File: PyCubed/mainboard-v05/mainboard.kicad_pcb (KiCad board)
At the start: 4 copper layers, 90.2 x 95.9 mm, 275 parts, among them J1 503182-1852, J10 Conn_01x04, J11 874370343, J12 Amphenol_901-144, J13 USB_C_pycubed, J14 Conn_01x06, J15 Conn_01x02, J16 1985807, J17 1985807, J18 1985807, J19 874370343, J2 Conn_01x05, J20 874370343, J21 874370343, J22 874370343, J23 874370343, J24 MOLEX_Sherlock_2pos, J3 MOLEX_Sherlock_2pos, J4 874370443, J5 Amphenol_901-144, J6 Amphenol_901-144, J7 Amphenol_901-144, J8 Conn_01x09, J9 Conn_01x03, Q1 IRLML2803, Q10 MBT2222ADW1T1, Q11 MMDT2907, Q12 BSS138DWQ-7, Q13 BSS138DWQ-7, Q14 BSS138DWQ-7, Q15 MBT2222ADW1T1, Q16 MBT2222ADW1T1, Q17 MMBT2907, Q18 BSS138DWQ-7, Q19 BSS138DWQ-7, Q2 MBT2222ADW1T1, Q20 NDS8434, Q21 NDS8434, Q22 NDS8434, Q23 MBT2222ADW1T1, Q24 BSS138DWQ-7, Q25 MBT2222ADW1T1, Q26 BSS138DWQ-7, Q27 MBT2222ADW1T1, Q3 MBT2222ADW1T1, Q4 IRLML2803, Q5 IRLML2803, Q6 MMBT2222AT, Q7 MBT2222ADW1T1, Q8 MBT2222ADW1T1, Q9 BSS138DWQ-7, SW1 KMR231NG LFS, U1 MAX706RESA, U13 EP2W+, U14 S1216V8, U15 RFM9xBreakout, U16 PE014006, U17 BQ25883RGER, U2 ATSAMD51J19A-AU, U21 TPS7A4501DCQT, U23 RFM98PW, U24 RFM98PW, U3 BMX160, U4 ADM1176-1ARMZ-R7, U5 TPS54226PWPRPWP14_2P31X2P46-L, U6 LTC4121, U7 KF50BD-TR, U8 MR25H40MDF, U9 TPS54226PWPRPWP14_2P31X2P46-L, Y1 32.768kHz

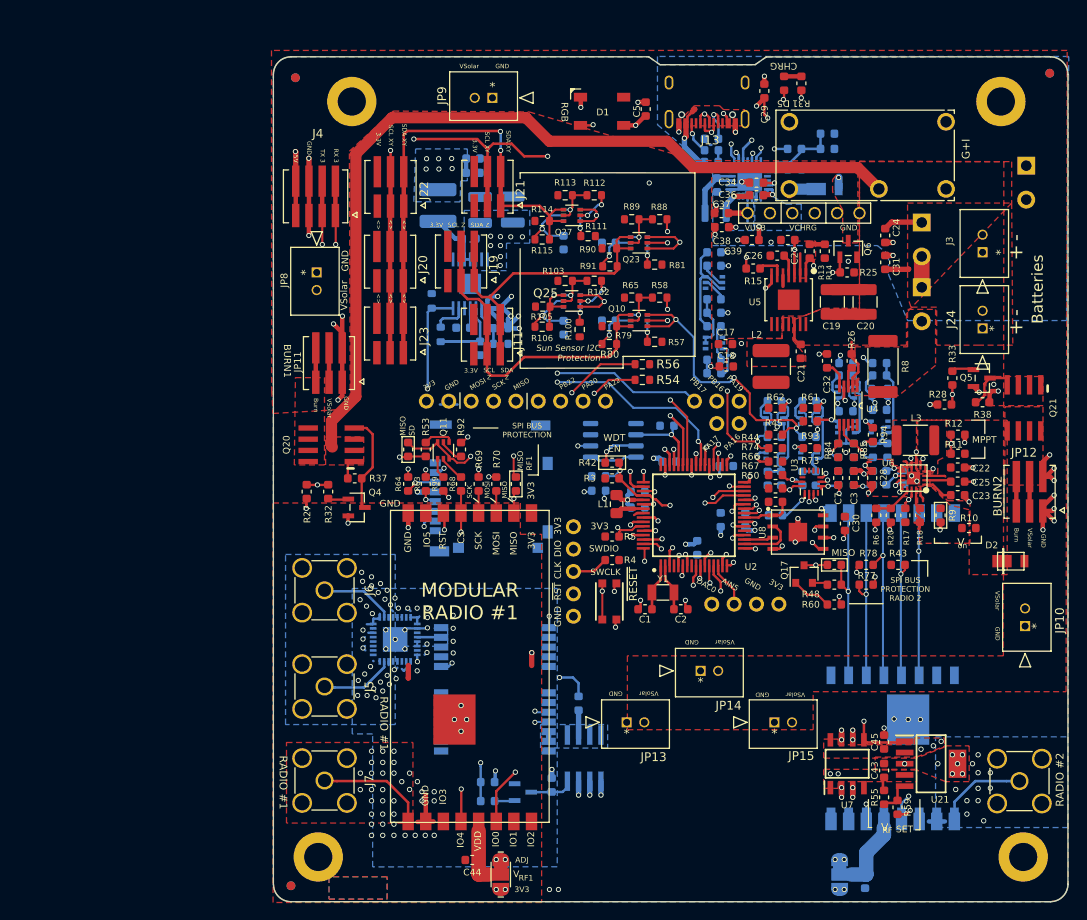
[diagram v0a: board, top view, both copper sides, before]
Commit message: Battery board and side panels ready for CAD check and review, pycubed not finished yet
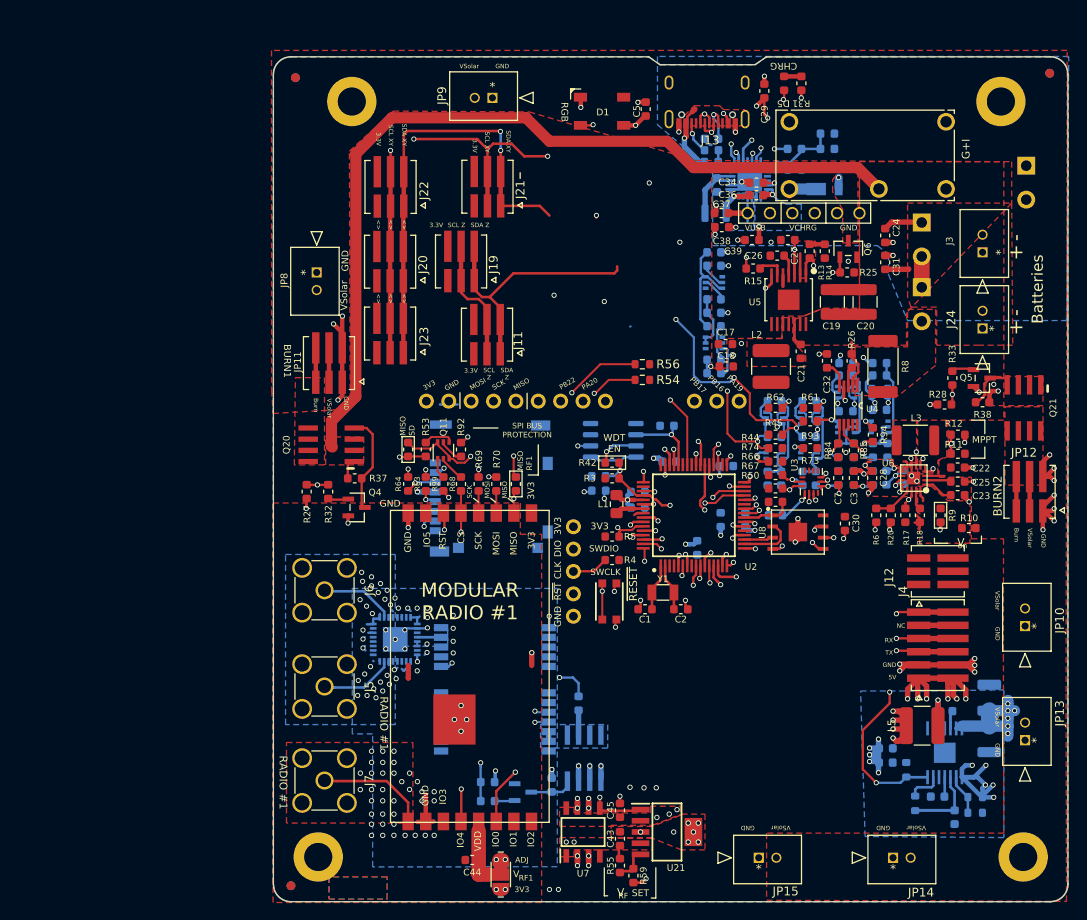
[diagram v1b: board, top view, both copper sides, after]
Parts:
- removed C46: 10uF, Capacitor_SMD:C_0603_1608Metric
- removed C47, C48, C49, C50: 10nF, Capacitor_SMD:C_0603_1608Metric
- removed D2: DFLS130L, mainboard:PWRDI-123
- removed J10: Conn_01x04, Connector_PinHeader_2.54mm:PinHeader_1x04_P2.54mm_Vertical
- removed J15: Conn_01x02, mainboard:PinHeader_CUSTOM3
- removed JP7: Jumper_3_Bridged12, mainboard:SolderJumper-3_P1.3mm_Bridged12_RoundedPad1.0x1.5mm
- removed Q10, Q23, Q25, Q27: MBT2222ADW1T1, Package_TO_SOT_SMD:SOT-363_SC-70-6
- removed Q14, Q24, Q26, Q9: BSS138DWQ-7, mainboard:BSS138DWQ-7
- removed Q17: MMBT2907, Package_TO_SOT_SMD:SOT-23
- removed R100, R111, R57, R81: 100K, Resistor_SMD:R_0603_1608Metric
- removed R102, R112, R58, R88: 680, Resistor_SMD:R_0603_1608Metric
- removed R103, R105, R113, R114, R65, R79, R89, R90: 10K, Resistor_SMD:R_0603_1608Metric
- removed R106, R115, R80, R91: 200K, Resistor_SMD:R_0603_1608Metric
- removed R107, R48: 0, Resistor_SMD:R_0603_1608Metric
- removed R43: 10k, Resistor_SMD:R_0603_1608Metric
- removed R60: 4.7k, Resistor_SMD:R_0603_1608Metric
- removed R77, R78: 1K, Resistor_SMD:R_0603_1608Metric
- removed U15: RFM9xBreakout, RF_Module:HOPERF_RFM9XW_SMD
- removed U24: RFM98PW, mainboard:RFM95PW
- J12: value Amphenol_901-144 -> 874370343; footprint Connector_Coaxial:SMA_Amphenol_901-144_Vertical -> mainboard:MOLEX_874370343
- J4: value 874370443 -> 874370643; footprint mainboard:MOLEX_874370443 -> mainboard:MOLEX_874370643
- L5: moved to F.Cu
- R54, R56: value 4.7K -> 10K
- moved J4 87.1 mm to (173.7, 119.3), turned to 90 degrees
- moved C51 81.7 mm to (167.9, 131.0)
- moved C52 81.7 mm to (167.8, 132.6)
- moved C54 80.8 mm to (179.6, 129.9), turned to 270 degrees
- moved L5 80.6 mm to (172.0, 128.4), turned to 180 degrees
- moved C53 80.0 mm to (179.6, 125.2)
- moved C55 76.2 mm to (174.6, 126.7)
- moved C56 75.7 mm to (173.7, 136.4)
- moved R118 75.7 mm to (178.0, 138.3)
- moved R119 75.7 mm to (171.2, 137.2)
- moved U9 75.7 mm to (174.5, 131.5)
- moved R116 75.7 mm to (170.2, 133.4)
- moved C57 75.7 mm to (175.6, 138.8)
- moved R117 75.7 mm to (178.0, 136.5)
- moved JP13 45.3 mm to (183.6, 130.0), turned to 270 degrees
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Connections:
- net THM renamed Net-(R34-Pad2)
- C22 pad 1: /Power/VCHRG_IN -> VSOLAR
- J11 pad 1_1: SDA_SS_Z -> SDA
- J11 pad 1_2: SDA_SS_Z -> SDA
- J11 pad 2_1: SCL_SS_Z -> SCL
- J11 pad 2_2: SCL_SS_Z -> SCL
- J19 pad 1_1: SDA_SS_Z -> SDA
- J19 pad 1_2: SDA_SS_Z -> SDA
- J19 pad 2_1: SCL_SS_Z -> SCL
- J19 pad 2_2: SCL_SS_Z -> SCL
- J20 pad 1_1: SDA_SS_XY -> SDA_2
- J20 pad 1_2: SDA_SS_XY -> SDA_2
- J20 pad 2_1: SCL_SS_XY -> SCL_2
- J20 pad 2_2: SCL_SS_XY -> SCL_2
- J21 pad 1_1: SDA_SS_XY -> SDA_2
- J21 pad 1_2: SDA_SS_XY -> SDA_2
- J21 pad 2_1: SCL_SS_XY -> SCL_2
- J21 pad 2_2: SCL_SS_XY -> SCL_2
- J22 pad 1_1: SDA_SS_XY -> SDA_2
- J22 pad 1_2: SDA_SS_XY -> SDA_2
- J22 pad 2_1: SCL_SS_XY -> SCL_2
- J22 pad 2_2: SCL_SS_XY -> SCL_2
- J23 pad 1_1: SDA_SS_XY -> SDA_2
- J23 pad 1_2: SDA_SS_XY -> SDA_2
- J23 pad 2_1: SCL_SS_XY -> SCL_2
- J23 pad 2_2: SCL_SS_XY -> SCL_2
- J4 pad 1_1: PB17 -> 5V
- J4 pad 1_2: PB17 -> 5V
- J4 pad 2_1: PB16 -> GND
- J4 pad 2_2: PB16 -> GND
- J4 pad 3_1: GND -> TX_2
- J4 pad 3_2: GND -> TX_2
- J4 pad 4_1: 5V -> RX_2
- J4 pad 4_2: 5V -> RX_2
- J8 pad 8: PA20 -> PB14
- J8 pad 9: PA22 -> (no net)
- J9 pad 3: PA19 -> (no net)
- R10 pad 2: /Power/VCHRG_IN -> VSOLAR
- R11 pad 2: /Power/VCHRG_IN -> VSOLAR
- R116 pad 2: PB23 -> ENAB_CORAL
- R54 pad 2: PA17 -> SCL_2
- R56 pad 2: PA16 -> SDA_2
- U14 pad 22: GPS_PWR_IN -> Net-(U14-Pad22)
- U14 pad 23: GPS_PWR_IN -> Net-(U14-Pad22)
- U2 pad 10: RF2_IO4 -> ENAB_CORAL
- U2 pad 12: RF2_CS -> RST_CORAL
- U2 pad 13: ENAB_RF -> TX_2
- U2 pad 14: AIN5 -> RX_2
- U2 pad 27: RF2_RST -> PB14
- U2 pad 3: DAC0 -> SENSE_THERM
- U2 pad 35: PA16 -> SDA_2
- U2 pad 36: PA17 -> SCL_2
- U2 pad 38: PA19 -> ENAB_RF
- U2 pad 41: PA20 -> (no net)
- U2 pad 43: PA22 -> (no net)
- U2 pad 50: PB23 -> (no net)
- U2 pad 9: RF2_IO0 -> ENAB_THERM
- U6 pad P$3: /Power/VCHRG_IN -> VSOLAR
- U9 pad 7: PB23 -> ENAB_CORAL
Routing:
- net SCL_2: track 0.00 -> 107.9 mm, vias 0 -> 7
- net SDA_2: track 0.00 -> 106.6 mm, vias 0 -> 5
- net SCL_SS_XY: track 76.3 -> 0.00 mm, vias 4 -> 0
- net PB16: track 72.9 -> 8.30 mm, vias 3 -> 1
- net PA16: track 63.9 -> 0.00 mm, vias 3 -> 0
- net PB17: track 67.8 -> 7.61 mm, vias 3 -> 1
- net SDA_SS_XY: track 58.2 -> 0.00 mm, vias 2 -> 0
- net RF2_RST: track 53.6 -> 0.00 mm, vias 2 -> 0
- net ENAB_CORAL: track 0.00 -> 49.6 mm, vias 0 -> 3
- net RF2_CS: track 46.5 -> 0.00 mm, vias 3 -> 0
- net PA17: track 46.4 -> 0.00 mm, vias 3 -> 0
- net PB23: track 44.0 -> 0.00 mm, vias 2 -> 0
- net /Power/V_RF: track 55.0 -> 11.1 mm, vias 6 -> 4
- net RF2_IO4: track 41.8 -> 0.00 mm, vias 2 -> 0
- net SCL_SS_Z: track 39.1 -> 0.00 mm
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- removed copper zone on F.Cu, net /Power/VCHRG_IN
- removed copper zone on B.Cu, net VBATT
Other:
- board text added: "NC"
- board text added: "RX"
- board text added: "TX"
- board text removed: "AIN5"
- board text removed: "ANT"
- board text removed: "DAC0"
- board text removed: "MODULAR RADIO #2"
- board text removed: "PA16"
- board text removed: "PA17"
- board text removed: "PA22"
- board text removed: "RADIO #2"
- board text removed: "RF2"
- board text removed: "RX 3"
- board text removed: "SPI BUS PROTECTION RADIO 2"
- board text removed: "Sun Sensor I2C Protection"
- board text removed: "TX 3"

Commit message: side panels ready except for RF trace width
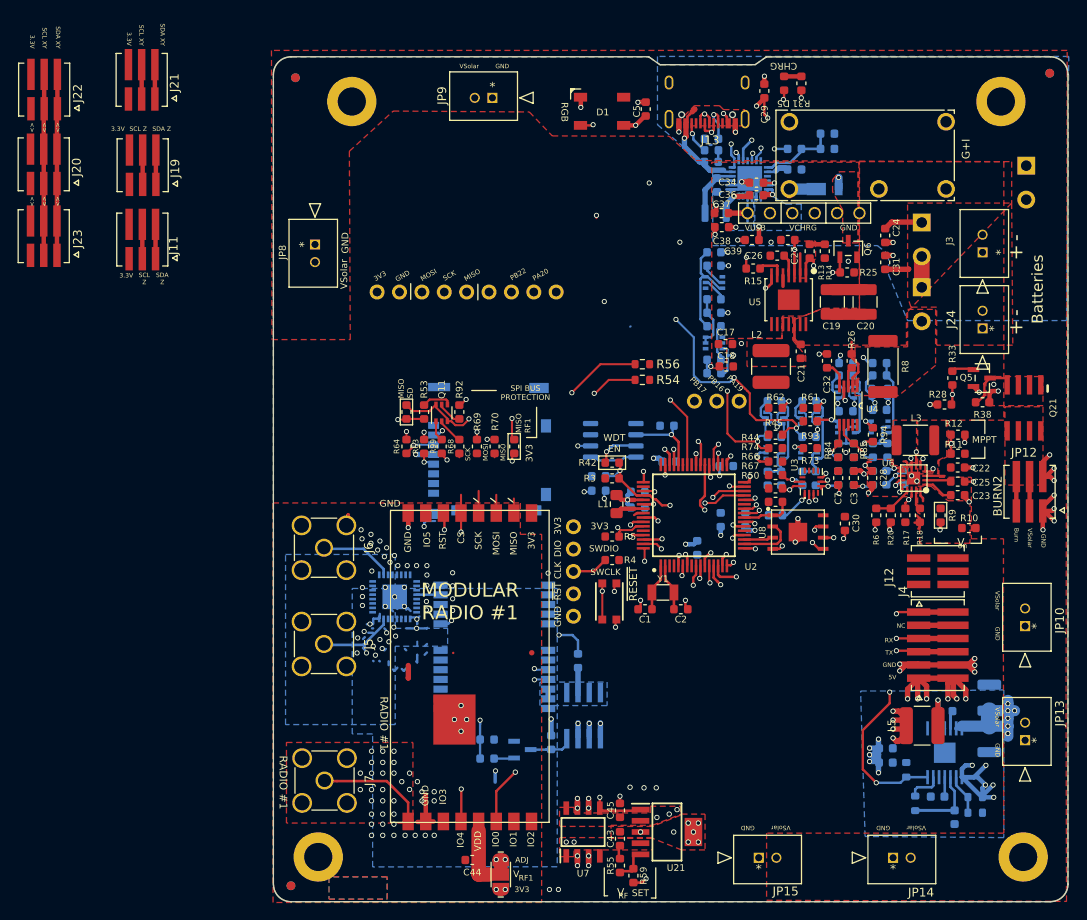
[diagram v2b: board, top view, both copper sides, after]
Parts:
- removed JP11: 874370343, mainboard:MOLEX_874370343
- removed Q20: NDS8434, mainboard:NDS8434
- removed Q4: IRLML2803, mainboard:SOT-23
- removed R27: 10k, Resistor_SMD:R_0603_1608Metric
- removed R32: 4.7k, Resistor_SMD:R_0603_1608Metric
- removed R37: 100k, Resistor_SMD:R_0603_1608Metric
- moved J21 41.1 mm to (83.4, 55.1)
- moved J20 40.8 mm to (72.3, 64.7)
- moved J22 40.8 mm to (72.3, 56.2)
- moved J23 40.8 mm to (72.3, 72.8)
- moved J11 40.6 mm to (83.5, 73.2)
- moved J19 37.7 mm to (83.5, 64.8)
- moved J8 13.6 mm to (110.1, 79.2)
- moved J6 4.83 mm to (111.7, 108.2)
- moved Q22 4.83 mm to (133.5, 127.3)
- moved U13 4.83 mm to (112.1, 113.8)
- moved J5 4.83 mm to (111.7, 119.1)
- moved Q1 4.83 mm to (126.7, 131.1)
- moved R21 4.83 mm to (122.6, 130.0)
- moved R22 4.83 mm to (122.6, 132.1)
- moved R23 4.83 mm to (129.9, 130.3)
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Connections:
- U2 pad 60: ENAB_BURN1 -> (no net)
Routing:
- net /Burn Wires/VBURN_A_IN: track 133.8 -> 33.1 mm
- net ENAB_BURN1: track 49.2 -> 0.00 mm, vias 2 -> 0
- net SCL_2: track 107.9 -> 62.4 mm, vias 7 -> 3
- net RF1_IO4: track 43.6 -> 10.9 mm
- net SDA_2: track 106.6 -> 79.6 mm, vias 5 -> 3
- net RF1_IO0: track 37.9 -> 11.8 mm
- net SDA: track 98.3 -> 76.0 mm
- net GND: track 126.0 -> 106.3 mm, vias 168 -> 160
- net SCK: track 51.5 -> 34.9 mm
- net MOSI: track 54.1 -> 38.0 mm
- net MISO: track 53.3 -> 39.4 mm
- net Net-(Q20-Pad4): track 11.4 -> 0.00 mm
- net SCL: track 76.3 -> 69.9 mm
- net PB22: track 15.1 -> 9.75 mm
- net (no net): track 0.06 -> 5.14 mm
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- removed copper zone on F.Cu, net /Burn Wires/VBURN1
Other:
- board text removed: "BURN1"

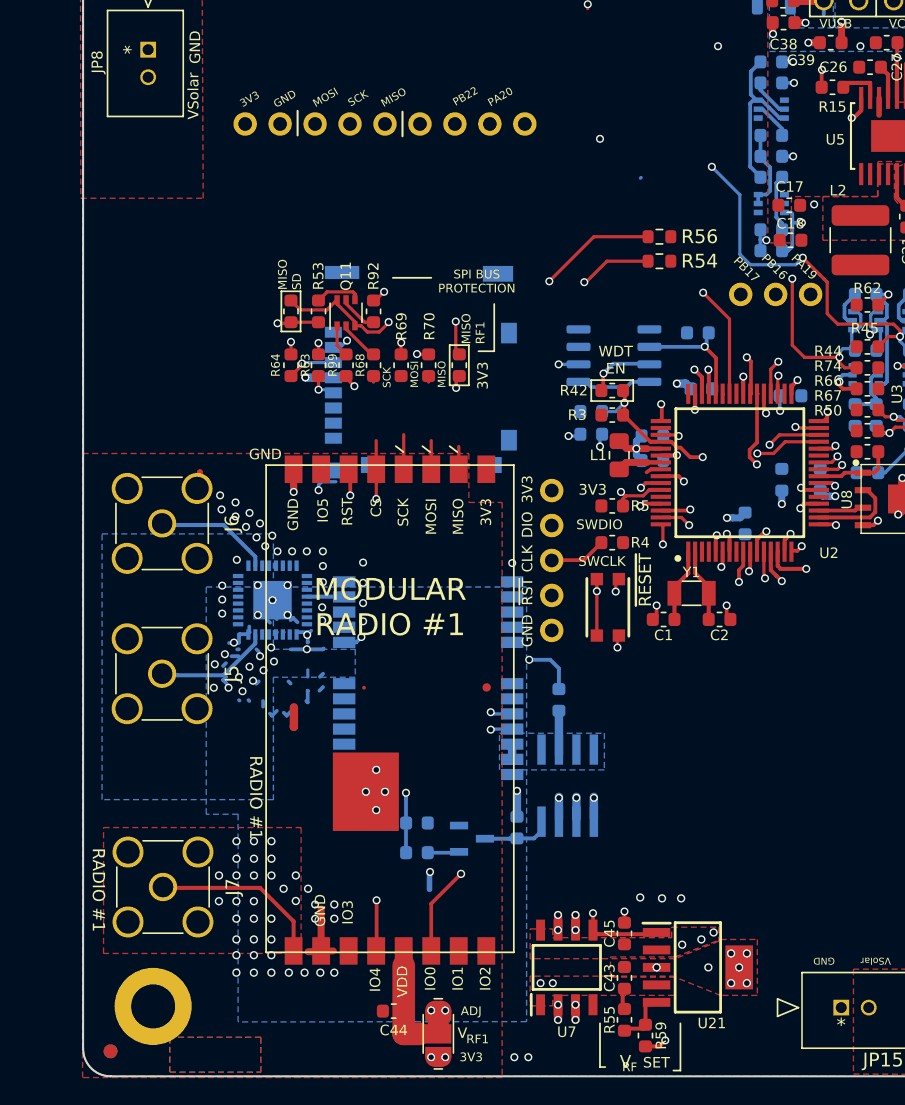
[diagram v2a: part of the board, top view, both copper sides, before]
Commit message: radio and gps moved to make space for limit switches
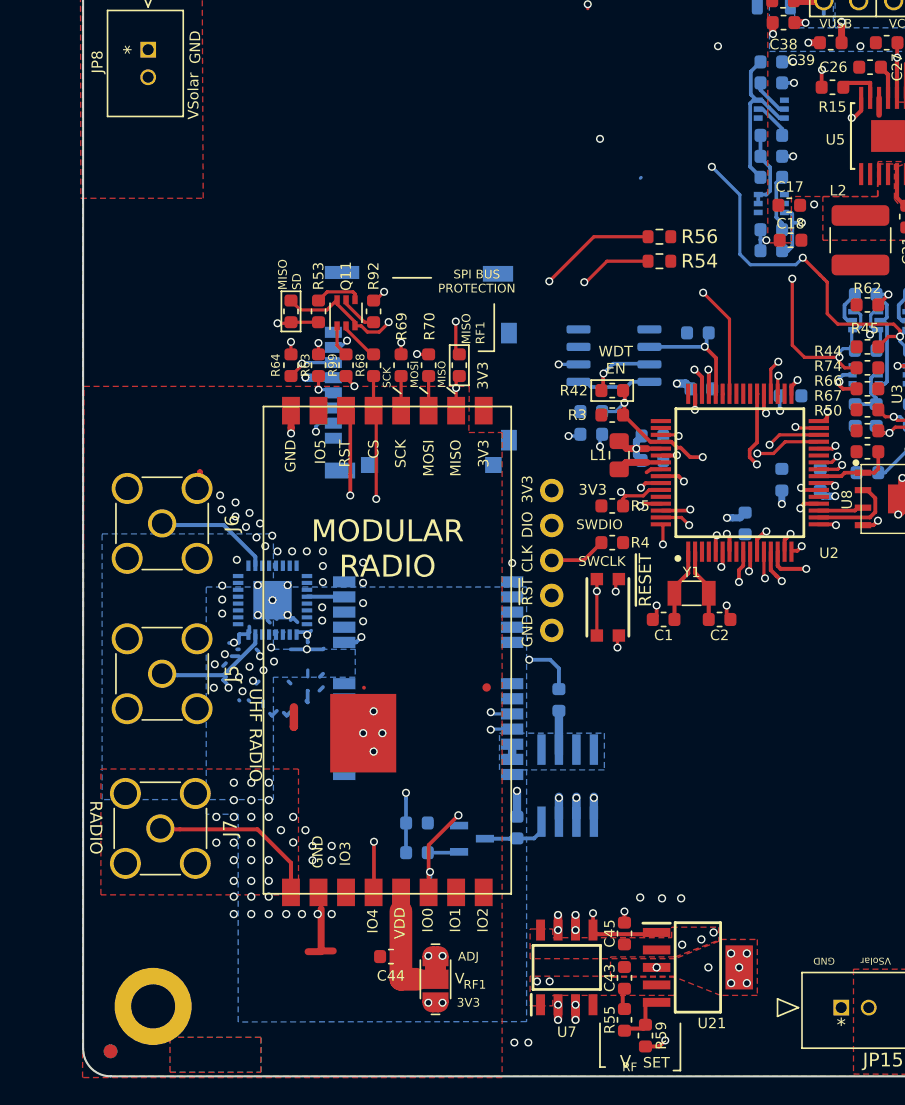
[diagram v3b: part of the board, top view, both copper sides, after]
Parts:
- removed J8: Conn_01x09, Connector_PinHeader_2.54mm:PinHeader_1x09_P2.54mm_Vertical
- removed J9: Conn_01x03, Connector_PinHeader_2.54mm:PinHeader_1x03_P2.54mm_Vertical
- moved J7 4.26 mm to (111.6, 130.4)
- moved U23 4.26 mm to (120.9, 117.4)
- moved C44 3.97 mm to (120.7, 139.7)
- moved JP6 3.97 mm to (123.9, 141.3)
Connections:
- U2 pad 27: PB14 -> (no net)
- U2 pad 39: PB16 -> (no net)
- U2 pad 40: PB17 -> (no net)
- U2 pad 49: PB22 -> (no net)
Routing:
- net RF1_IO4: track 10.9 -> 42.1 mm
- net RF1_IO0: track 11.8 -> 37.6 mm, vias 2 -> 3
- net SCK: track 34.9 -> 45.6 mm
- net MOSI: track 38.0 -> 48.1 mm
- net PB22: track 9.75 -> 0.00 mm, vias 1 -> 0
- net MISO: track 39.4 -> 49.2 mm
- net SD_CS: track 29.0 -> 38.6 mm
- net PB16: track 8.30 -> 0.00 mm, vias 1 -> 0
- net PB17: track 7.61 -> 0.00 mm, vias 1 -> 0
- net RF1_RST: track 26.9 -> 31.5 mm
- net RF1_CS: track 27.2 -> 31.7 mm
- net 3.3V: track 78.4 -> 79.8 mm
- net GND: track 106.3 -> 105.1 mm, vias 160 -> 159
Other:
- board text added: "MODULAR RADIO"
- board text added: "RADIO"
- board text added: "UHF RADIO"
- board text removed: "MODULAR RADIO #1"
- board text removed: "PA19"
- board text removed: "PA20"
- board text removed: "PB16"
- board text removed: "PB17"
- board text removed: "PB22"
- board text removed: "RADIO #1"

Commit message: pycubed finished, awaiting review
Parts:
- removed J12, JP12: 874370343, mainboard:MOLEX_874370343
- removed J17: 1985807, mainboard:SCREWTERMINAL-3.5MM-2_LOCK
- removed J24, JP10, JP13, JP14, JP15, JP8, JP9: MOLEX_Sherlock_2pos, mainboard:MOLEX_Sherlock_2pos
- added J8: 1985807, mainboard:SCREWTERMINAL-3.5MM-2_LOCK, F.Cu at (139.9, 72.4)
- added J9: 1985807, mainboard:SCREWTERMINAL-3.5MM-2_LOCK, F.Cu at (173.5, 72.9)
- added Ref**: Val**, mainboard:board_info_block_bot, F.Cu at (151.1, 128.7)
- added Ref**: Val**, mainboard:XYZ_cubesat-bot, B.Cu at (160.5, 118.2)
- J11, J19, J20, J21, J22, J23: value 874370343 -> 35362-0650; footprint mainboard:MOLEX_874370343 -> mainboard:MOLEX_35362-0650
- J16, J18: moved to F.Cu
- J3: value MOLEX_Sherlock_2pos -> 35362-0650; footprint mainboard:MOLEX_Sherlock_2pos -> mainboard:MOLEX_35362-0650
- J4: value 874370643 -> 35362-0650; footprint mainboard:MOLEX_874370643 -> mainboard:MOLEX_35362-0650
- moved J19 104.9 mm to (157.5, 139.1)
- moved J11 104.4 mm to (183.1, 104.3), turned to 270 degrees
- moved J22 48.8 mm to (120.4, 64.8), turned to 0 degrees
- moved J21 46.6 mm to (120.4, 83.3)
- moved J18 46.3 mm to (140.0, 80.0)
- moved J23 37.9 mm to (104.9, 92.1), turned to 90 degrees
- moved J20 34.4 mm to (104.9, 75.5), turned to 90 degrees
- moved J16 8.89 mm to (173.5, 80.2)
- moved J3 5.07 mm to (182.5, 78.2)
- moved J4 2.37 mm to (174.6, 117.0), turned to 270 degrees
- moved R41 1.08 mm to (156.1, 105.3), turned to 270 degrees
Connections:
- net ENAB_BURN2 renamed ENAB_BURN
- J16 pad 2: Net-(J16-Pad2) -> VBATT_SENSE
- Q21 pad 5: /Burn Wires/VBURN2 -> BURN
- Q21 pad 6: /Burn Wires/VBURN2 -> BURN
- Q21 pad 7: /Burn Wires/VBURN2 -> BURN
- Q21 pad 8: /Burn Wires/VBURN2 -> BURN
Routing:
- net SENSE_THERM: track 0.00 -> 104.4 mm, vias 0 -> 7
- net ENAB_THERM: track 2.40 -> 89.4 mm, vias 1 -> 4
- net SCL_2: track 62.4 -> 101.5 mm, vias 3 -> 2
- net SCL: track 69.9 -> 107.7 mm
- net GND: track 105.1 -> 74.8 mm, vias 159 -> 147
- net SDA: track 76.0 -> 106.1 mm
- net SDA_2: track 79.6 -> 106.4 mm
- net 5V: track 55.6 -> 35.6 mm, vias 20 -> 14
- net VBATT: track 95.8 -> 114.7 mm
- net VSOLAR: track 6.10 -> 24.5 mm
- net GNDREF: track 13.6 -> 26.3 mm
- net 3.3V: track 79.8 -> 92.3 mm
- net VBATT_SENSE: track 0.94 -> 10.8 mm
- net VCHRG: track 21.0 -> 25.5 mm, vias 0 -> 1
- net Net-(J4-Pad5_1): track 3.90 -> 0.00 mm
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- added copper zone on F.Cu, net BURN
- removed copper zone on F.Cu, net /Burn Wires/VBURN2
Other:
- outline, holes or cut-outs redrawn
- board text added: "Battery Board Connection"
- board text added: "Google Coral Connection"
- board text added: "Low Side Switches"
- board text added: "RST_Coral"
- board text added: "SCL"
- board text added: "SDA"
- board text added: "Therm"
- board text added: "X / Y Side Panel Connection"
- board text added: "Z+ Side Panel Connection - Burn Wire"
- board text added: "Z- Side Panel Connection"
- board text removed: "<>"
- board text removed: "BURN2"
- board text removed: "Batteries"
- board text removed: "Low Side Switch"
- board text removed: "NC"
- board text removed: "RGB"
- board text removed: "SCL XY"
- board text removed: "SCL Z"
- board text removed: "SDA XY"
- board text removed: "SDA Z"
